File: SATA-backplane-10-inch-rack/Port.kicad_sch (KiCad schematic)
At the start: 2 parts, among them J201 67800-5001, J202 1735284-2

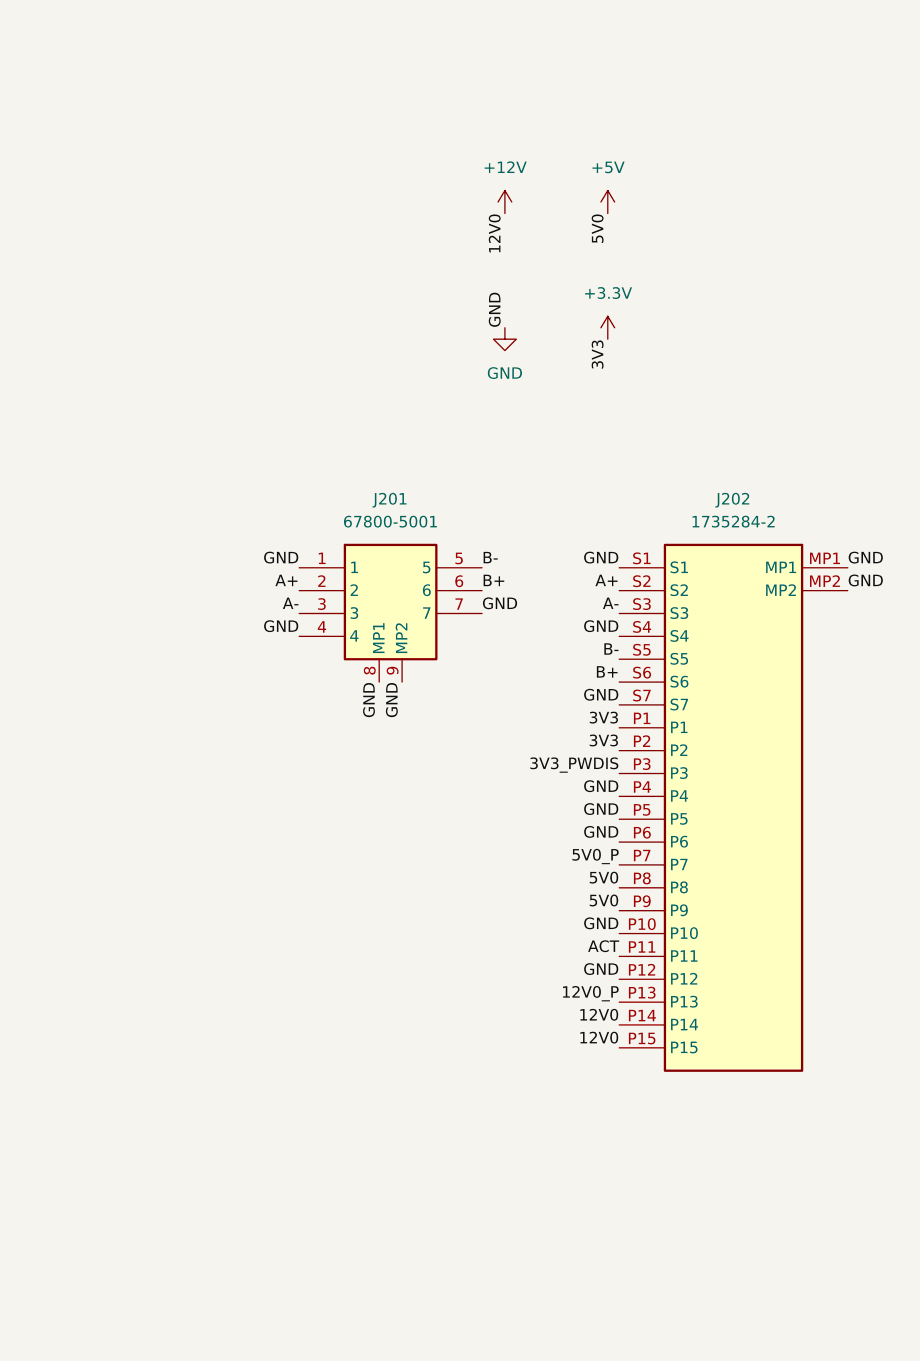
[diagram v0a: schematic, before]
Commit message: More realistic layout
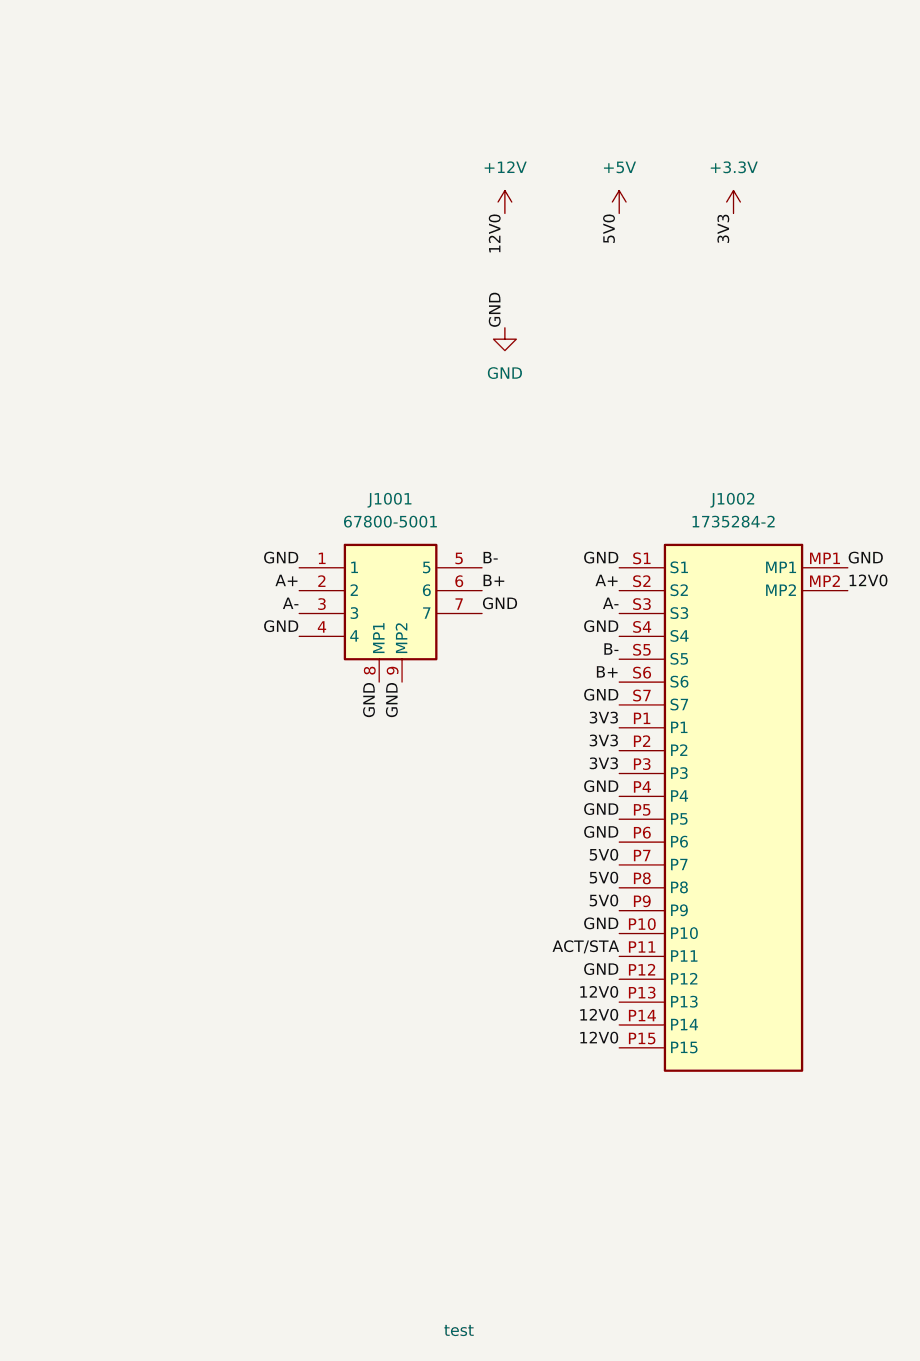
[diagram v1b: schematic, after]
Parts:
- J1001: renamed from J201; Mouser Price/Stock https://www.mouser.co.uk/ProductDetail/Molex/67800-5001?qs=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 -> (none)
- J1002: renamed from J202; Arrow Part Number 1735284-2 -> (none); Arrow Price/Stock https://www.arrow.com/en/products/1735284-2/te-connectivity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 -> (none); Height 9.95 -> (none); Mouser Price/Stock https://www.mouser.co.uk/ProductDetail/TE-Connectivity/1735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 -> (none)
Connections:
- net 12V0_P is gone; now on net +12V: J1002.P13
- net 3V3_PWDIS is gone; now on net +3.3V: J1002.P3
- net 5V0_P is gone; now on net +5V: J1002.P7
- net +12V: now also J1002.MP2
- net GND: no longer J1002.MP2
- net ACT renamed ACT/STA
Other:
- note added: "test"
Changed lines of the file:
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@@
 	(generator_version "8.0")
 	(paper "A4")
+	(text "test"
+		(exclude_from_sim no)
+		(at 101.5762 171.3654 0)
+		(effects
+			(font
+				(size 1.27 1.27)
+			)
+		)
+	)
 	(label "GND"
 		(at 119.38 86.36 180)
@@
 		)
 	)
-	(label "5V0_P"
-		(at 119.38 119.38 180)
-		(fields_autoplaced yes)
-		(effects
-			(font
-				(size 1.27 1.27)
-			)
-			(justify right bottom)
-		)
-	)
 	(label "A+"
 		(at 119.38 88.9 180)
@@
 		)
 	)
-	(label "3V3_PWDIS"
-		(at 119.38 109.22 180)
-		(fields_autoplaced yes)
-		(effects
-			(font
-				(size 1.27 1.27)
-			)
-			(justify right bottom)
-		)
-	)
 	(label "GND"
 		(at 95.25 99.06 270)
@@
 		)
 	)
-	(label "12V0_P"
-		(at 119.38 134.62 180)
-		(fields_autoplaced yes)
-		(effects
-			(font
-				(size 1.27 1.27)
-			)
-			(justify right bottom)
-		)
-	)
 	(label "5V0"
 		(at 119.38 121.92 180)
@@
 		)
 	)
+	(label "3V3"
+		(at 119.38 109.22 180)
+		(fields_autoplaced yes)
+		(effects
+			(font
+				(size 1.27 1.27)
+			)
+			(justify right bottom)
+		)
+	)
 	(label "12V0"
 		(at 106.68 46.99 270)
@@
 		)
 	)
+	(label "12V0"
+		(at 119.38 134.62 180)
+		(fields_autoplaced yes)
+		(effects
+			(font
+				(size 1.27 1.27)
+			)
+			(justify right bottom)
+		)
+	)
 	(label "A-"
 		(at 119.38 91.44 180)
@@
 		)
 	)
+	(label "5V0"
+		(at 119.38 119.38 180)
+		(fields_autoplaced yes)
+		(effects
+			(font
+				(size 1.27 1.27)
+			)
+			(justify right bottom)
+		)
+	)
 	(label "GND"
 		(at 92.71 99.06 270)
@@
 		)
 	)
+	(label "12V0"
+		(at 144.78 88.9 0)
+		(fields_autoplaced yes)
+		(effects
+			(font
+				(size 1.27 1.27)
+			)
+			(justify left bottom)
+		)
+	)
 	(label "GND"
 		(at 119.38 93.98 180)
@@
 		)
 	)
-	(label "ACT"
+	(label "ACT{slash}STA"
 		(at 119.38 129.54 180)
 		(fields_autoplaced yes)
@@
 			)
 			(justify right bottom)
-		)
-	)
-	(label "GND"
-		(at 144.78 88.9 0)
-		(fields_autoplaced yes)
-		(effects
-			(font
-				(size 1.27 1.27)
-			)
-			(justify left bottom)
 		)
 	)
@@
 	)
 	(label "5V0"
-		(at 118.11 46.99 270)
+		(at 119.38 46.99 270)
 		(fields_autoplaced yes)
 		(effects
@@
 	)
 	(label "3V3"
-		(at 118.11 60.96 270)
+		(at 132.08 46.99 270)
 		(fields_autoplaced yes)
 		(effects
@@
 		(dnp no)
 		(fields_autoplaced yes)
-		(property "Reference" "J201"
+		(property "Reference" "J1001"
 			(at 93.98 78.74 0)
 			(effects
@@
 			)
 		)
-		(property "Height" ""
-			(at 100.33 481.28 0)
-			(effects
-				(font
-					(size 1.27 1.27)
-				)
-				(justify left top)
-				(hide yes)
-			)
-		)
 		(property "Manufacturer_Name" "Molex"
 			(at 100.33 581.28 0)
@@
 		(property "Mouser Part Number" "538-67800-5001"
 			(at 100.33 781.28 0)
-			(effects
-				(font
-					(size 1.27 1.27)
-				)
-				(justify left top)
-				(hide yes)
-			)
-		)
-		(property "Mouser Price/Stock" "https://www.mouser.co.uk/ProductDetail/Molex/67800-5001?qs=g5f4E6w8l8gZOK2cvWxb3Q%3D%3D"
-			(at 100.33 881.28 0)
-			(effects
-				(font
-					(size 1.27 1.27)
-				)
-				(justify left top)
-				(hide yes)
-			)
-		)
-		(property "Arrow Part Number" ""
-			(at 100.33 981.28 0)
-			(effects
-				(font
-					(size 1.27 1.27)
-				)
-				(justify left top)
-				(hide yes)
-			)
-		)
-		(property "Arrow Price/Stock" ""
-			(at 100.33 1081.28 0)
 			(effects
 				(font
@@
 		(dnp no)
 		(fields_autoplaced yes)
-		(property "Reference" "#PWR0201"
+		(property "Reference" "#PWR01001"
 			(at 106.68 50.8 0)
 			(effects
@@
 		(dnp no)
 		(fields_autoplaced yes)
-		(property "Reference" "J202"
+		(property "Reference" "J1002"
 			(at 132.08 78.74 0)
 			(effects
@@
 			)
 		)
-		(property "Height" "9.95"
-			(at 123.19 481.28 0)
-			(effects
-				(font
-					(size 1.27 1.27)
-				)
-				(justify left top)
-				(hide yes)
-			)
-		)
 		(property "Manufacturer_Name" "TE Connectivity"
 			(at 123.19 581.28 0)
@@
 		(property "Mouser Part Number" "571-1735284-2"
 			(at 123.19 781.28 0)
-			(effects
-				(font
-					(size 1.27 1.27)
-				)
-				(justify left top)
-				(hide yes)
-			)
-		)
-		(property "Mouser Price/Stock" "https://www.mouser.co.uk/ProductDetail/TE-Connectivity/1735284-2?qs=p6VZ%252BklCkRRAA6jdGSMntw%3D%3D"
-			(at 123.19 881.28 0)
-			(effects
-				(font
-					(size 1.27 1.27)
-				)
-				(justify left top)
-				(hide yes)
-			)
-		)
-		(property "Arrow Part Number" "1735284-2"
-			(at 123.19 981.28 0)
-			(effects
-				(font
-					(size 1.27 1.27)
-				)
-				(justify left top)
-				(hide yes)
-			)
-		)
-		(property "Arrow Price/Stock" "https://www.arrow.com/en/products/1735284-2/te-connectivity?region=nac"
-			(at 123.19 1081.28 0)
 			(effects
 				(font
@@
 	(symbol
 		(lib_id "power:+3.3V")
-		(at 118.11 60.96 0)
+		(at 132.08 46.99 0)
 		(mirror y)
 		(unit 1)
@@
 		(dnp no)
 		(fields_autoplaced yes)
-		(property "Reference" "#PWR0204"
-			(at 118.11 64.77 0)
+		(property "Reference" "#PWR01004"
+			(at 132.08 50.8 0)
 			(effects
 				(font
@@
 		)
 		(property "Value" "+3.3V"
-			(at 118.11 55.88 0)
+			(at 132.08 41.91 0)
 			(effects
 				(font
@@
 		)
 		(property "Footprint" ""
-			(at 118.11 60.96 0)
+			(at 132.08 46.99 0)
 			(effects
 				(font
@@
 		)
 		(property "Datasheet" ""
-			(at 118.11 60.96 0)
+			(at 132.08 46.99 0)
 			(effects
 				(font
@@
 		)
 		(property "Description" "Power symbol creates a global label with name \"+3.3V\""
-			(at 118.11 60.96 0)
+			(at 132.08 46.99 0)
 			(effects
 				(font
@@
 		(dnp no)
 		(fields_autoplaced yes)
-		(property "Reference" "#PWR0203"
+		(property "Reference" "#PWR01003"
 			(at 106.68 66.04 0)
 			(effects
@@
 	(symbol
 		(lib_id "power:+5V")
-		(at 118.11 46.99 0)
+		(at 119.38 46.99 0)
 		(mirror y)
 		(unit 1)
@@
 		(dnp no)
 		(fields_autoplaced yes)
-		(property "Reference" "#PWR0202"
-			(at 118.11 50.8 0)
+		(property "Reference" "#PWR01002"
+			(at 119.38 50.8 0)
 			(effects
 				(font
@@
 		)
 		(property "Value" "+5V"
-			(at 118.11 41.91 0)
+			(at 119.38 41.91 0)
 			(effects
 				(font
@@
 		)
 		(property "Footprint" ""
-			(at 118.11 46.99 0)
+			(at 119.38 46.99 0)
 			(effects
 				(font
@@
 		)
 		(property "Datasheet" ""
-			(at 118.11 46.99 0)
+			(at 119.38 46.99 0)
 			(effects
 				(font
@@
 		)
 		(property "Description" "Power symbol creates a global label with name \"+5V\""
-			(at 118.11 46.99 0)
-			(effects
-				(font
+			(at 119.38 46.99 0)
+			(effects
+				(font

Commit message: STA/ACT implemented in layout
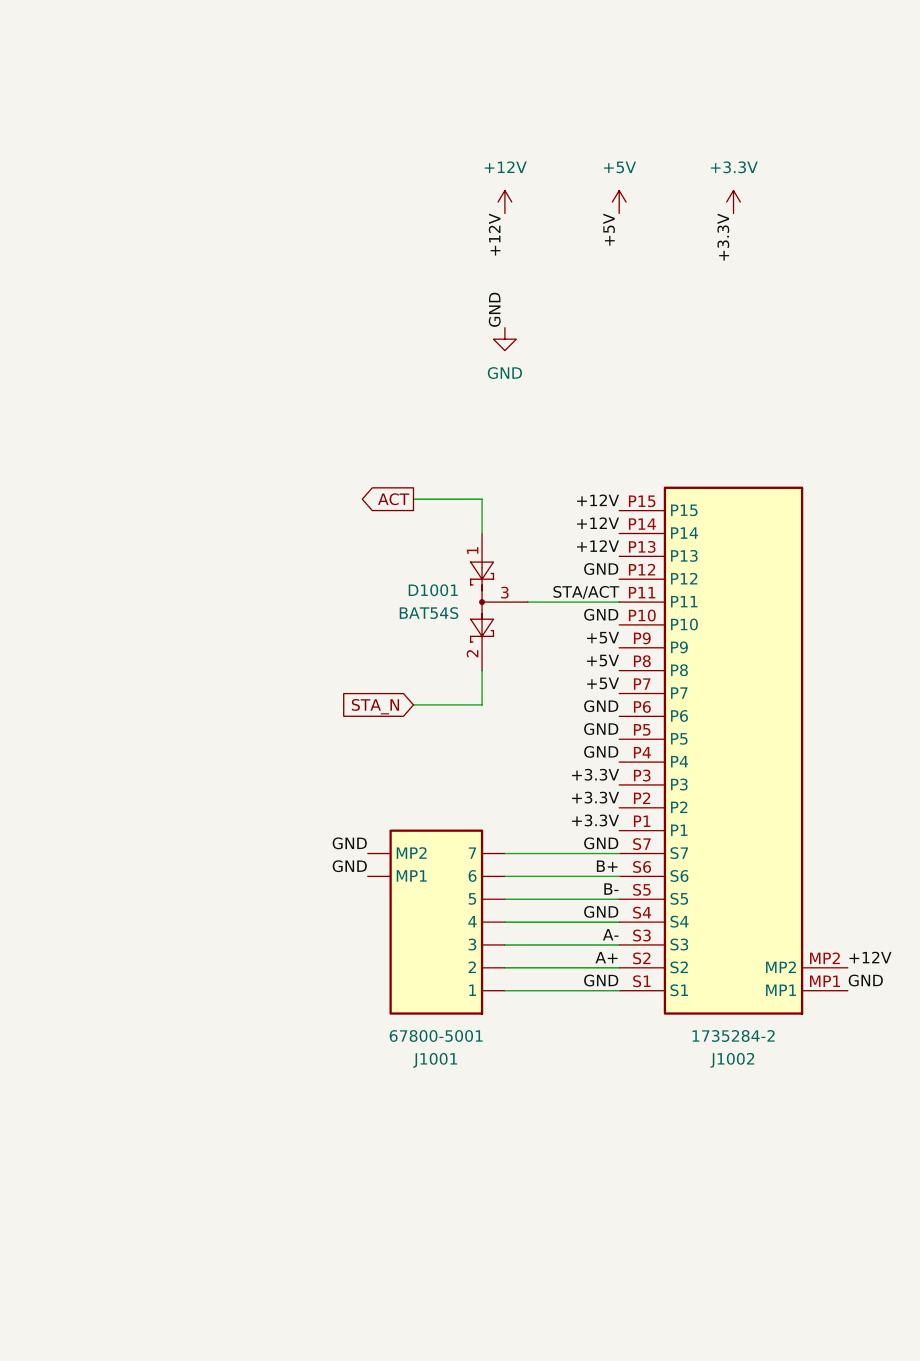
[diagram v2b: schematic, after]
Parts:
- added D1001: BAT54S, Package_TO_SOT_SMD:SOT-23, symbol Diode:BAT54S
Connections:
- net ACT/STA renamed STA/ACT
- net STA/ACT: now also D1001.3 (COM)
- new net ACT: D1001.1 (A)
- new net STA_N: D1001.2 (K)
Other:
- note removed: "test"
- moved on the sheet: J1002

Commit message: add capacitor discharge
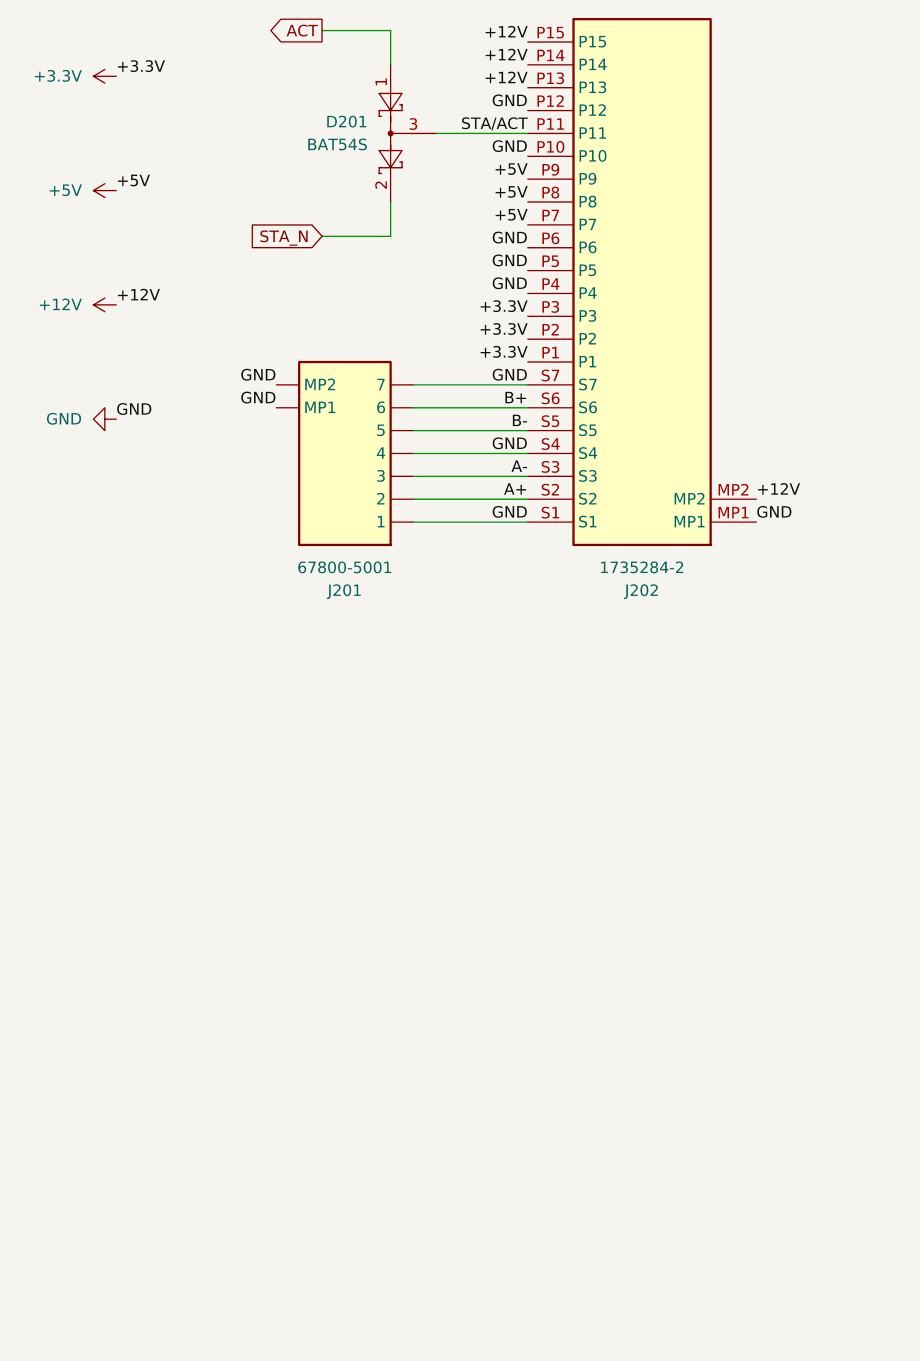
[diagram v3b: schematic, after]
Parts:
- renumbered D1001 to D201, J1001 to J201, J1002 to J202
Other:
- moved on the sheet: D201, J201, J202

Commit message: Fiddling with layout
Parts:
- D201: footprint Package_TO_SOT_SMD:SOT-23 -> Package_TO_SOT_SMD:SOT-23_Handsoldering; Mouser Part Number (none) -> 637-BAT54S
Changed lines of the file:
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@@
 			)
 		)
-		(property "Footprint" "Package_TO_SOT_SMD:SOT-23"
+		(property "Footprint" "Package_TO_SOT_SMD:SOT-23_Handsoldering"
 			(at 90.805 40.005 0)
 			(effects
@@
 			)
 		)
+		(property "Mouser Part Number" "637-BAT54S"
+			(at 93.98 38.1 0)
+			(effects
+				(font
+					(size 1.27 1.27)
+				)
+			)
+		)

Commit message: Place & Route
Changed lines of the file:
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@@
 		)
 		(property "Mouser Part Number" "637-BAT54S"
-			(at 93.98 38.1 0)
+			(at 91.44 40.6399 90)
 			(effects
 				(font
 					(size 1.27 1.27)
 				)
+				(justify left)
+				(hide yes)
 			)
 		)

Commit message: Schematic : define temporary mfg.partnumbers
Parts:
- D201: Manufacturer_Part_Number (none) -> BAT54S
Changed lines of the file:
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@@
+			)
+		)
+		(property "Manufacturer_Part_Number" "BAT54S"
+			(at 93.98 38.1 90)
+			(effects
+				(font
+					(size 1.27 1.27)
+				)
+				(hide yes)
 			)
 		)
